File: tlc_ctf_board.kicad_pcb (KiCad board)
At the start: 2 copper layers, 78 x 51 mm, 15 parts, among them J1 AVR-ISP-6, U1 ATtiny84A-SSU

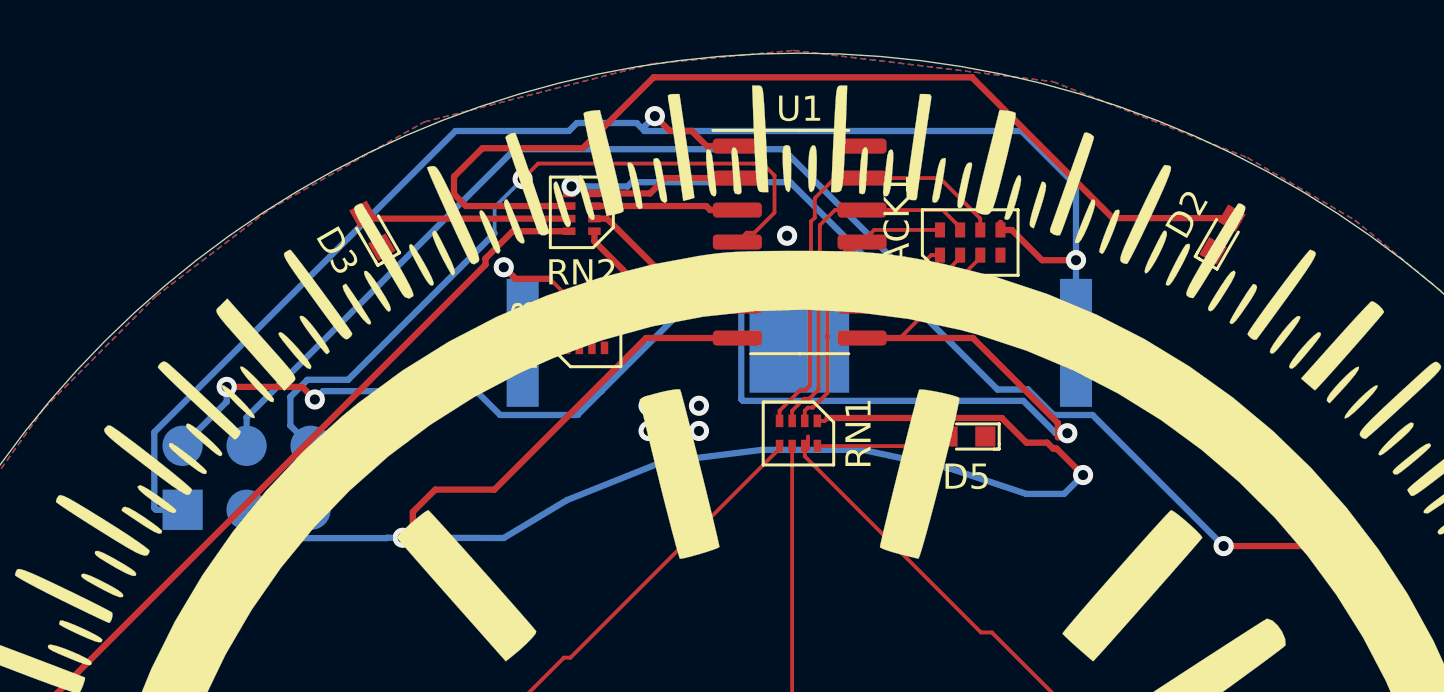
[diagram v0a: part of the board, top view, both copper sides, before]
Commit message: moved programming header
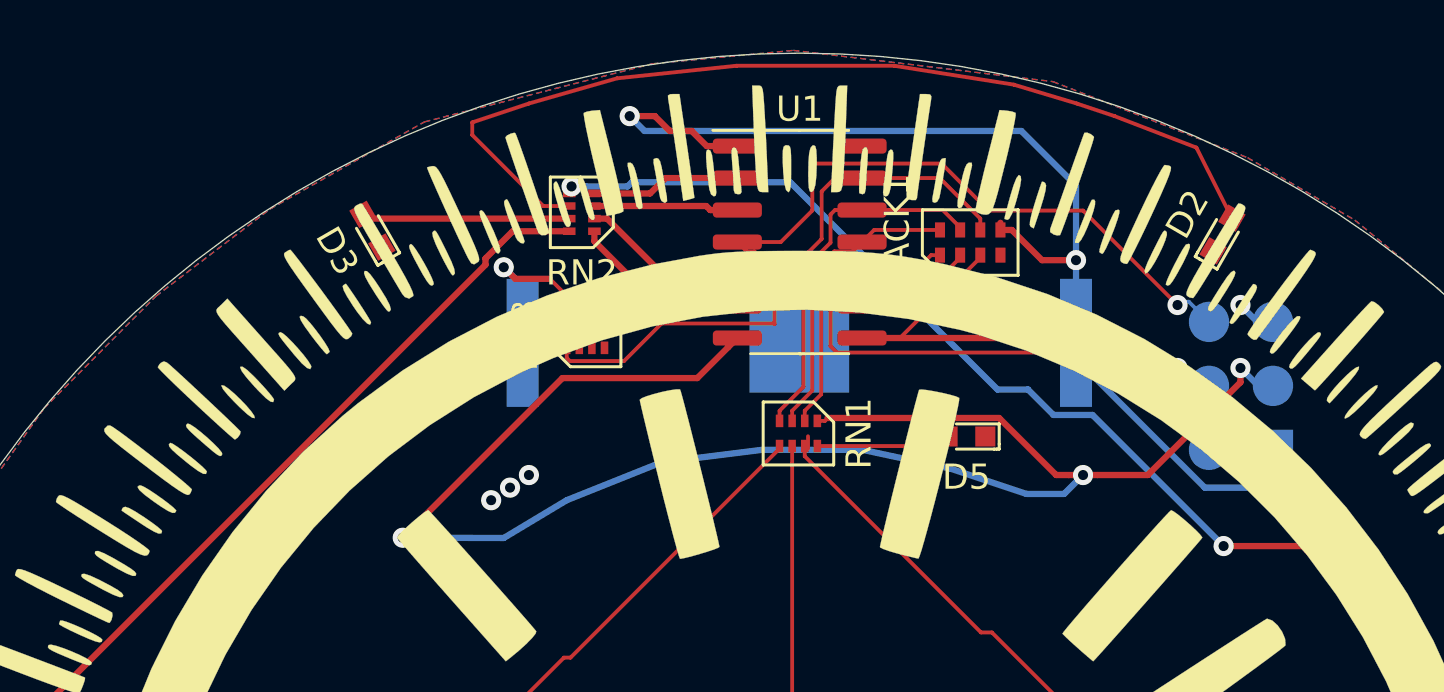
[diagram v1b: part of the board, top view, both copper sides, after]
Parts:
- moved J1 40.8 mm to (190.2, 57.2), turned to 0 degrees
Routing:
- net MISO: track 60.6 -> 22.4 mm, vias 3 -> 1
- net VCC: track 70.6 -> 54.6 mm
- net QT5: track 39.5 -> 25.7 mm, vias 0 -> 1
- net RESET: track 41.8 -> 37.6 mm, vias 2 -> 1
- net LED1: track 63.6 -> 66.5 mm, vias 2 -> 3
- net Net-(D2-Pad2): track 40.3 -> 38.2 mm
- net GND: track 0.00 -> 1.57 mm, vias 8 -> 4
